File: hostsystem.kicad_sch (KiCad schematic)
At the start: 75 parts, among them J1001 TC2050, J1002 Conn_01x03_Pin, U1001 AM6231ASGGGAALW, U1002 SN74LVC2G241DCUR, U1003 AT24C32D-STUM-T, X1001 32.768kHz, X1002 25MHz

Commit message: Added almost all passive component footprints
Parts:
- C1001, C1005, C1007: footprint (none) -> Capacitor_SMD:C_0201_0603Metric
- C1002, C1003, C1004, C1006, C1008, C1009: footprint (none) -> Capacitor_SMD:C_0402_1005Metric
- D1001, D1004, D1005, D1006: footprint (none) -> Diode_SMD:D_SOD-523
- D1002, D1003: footprint (none) -> Diode_SMD:D_SOD-882
- R1001, R1002, R1003, R1004, R1005, R1006, R1007, R1008, R1009, R1010, R1012, R1013, R1014, R1015, R1048, R1049, R1050, R1051: footprint (none) -> Resistor_SMD:R_0402_1005Metric
- R1011, R1016, R1017, R1018, R1019, R1020, R1021, R1022, R1023, R1024, R1025, R1026, R1027, R1028, R1029, R1030, R1031, R1032, R1033, R1034, R1035, R1036, R1037, R1038, R1039, R1040, R1041, R1042, R1043, R1044, R1045, R1046, R1047: footprint (none) -> Resistor_SMD:R_0201_0603Metric
- TP1001, TP1002: footprint (none) -> TestPoint:TestPoint_Pad_1.0x1.0mm
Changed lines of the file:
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@@
 			)
 		)
-		(property "Footprint" ""
+		(property "Footprint" "Resistor_SMD:R_0201_0603Metric"
 			(at 617.982 49.53 90)
 			(effects
@@
 			)
 		)
-		(property "Footprint" ""
+		(property "Footprint" "Resistor_SMD:R_0402_1005Metric"
 			(at 85.852 92.71 90)
 			(effects
@@
 			)
 		)
-		(property "Footprint" ""
+		(property "Footprint" "Resistor_SMD:R_0402_1005Metric"
 			(at 140.462 388.62 90)
 			(effects
@@
 			)
 		)
-		(property "Footprint" ""
+		(property "Footprint" "Resistor_SMD:R_0402_1005Metric"
 			(at 455.422 49.53 90)
 			(effects
@@
 			)
 		)
-		(property "Footprint" ""
+		(property "Footprint" "Resistor_SMD:R_0201_0603Metric"
 			(at 546.862 109.22 90)
 			(effects
@@
 			)
 		)
-		(property "Footprint" ""
+		(property "Footprint" "Resistor_SMD:R_0201_0603Metric"
 			(at 597.662 109.22 90)
 			(effects
@@
 			)
 		)
-		(property "Footprint" ""
+		(property "Footprint" "Resistor_SMD:R_0201_0603Metric"
 			(at 557.022 109.22 90)
 			(effects
@@
 			)
 		)
-		(property "Footprint" ""
+		(property "Footprint" "Diode_SMD:D_SOD-523"
 			(at 483.87 68.58 0)
 			(effects
@@
 			)
 		)
-		(property "Footprint" ""
+		(property "Footprint" "TestPoint:TestPoint_Pad_1.0x1.0mm"
 			(at 99.06 97.79 0)
 			(effects
@@
 			)
 		)
-		(property "Footprint" ""
+		(property "Footprint" "Resistor_SMD:R_0201_0603Metric"
 			(at 607.822 49.53 90)
 			(effects
@@
 			)
 		)
-		(property "Footprint" ""
+		(property "Footprint" "Capacitor_SMD:C_0402_1005Metric"
 			(at 191.4652 325.12 0)
 			(effects
@@
 			)
 		)
-		(property "Footprint" ""
+		(property "Footprint" "Resistor_SMD:R_0402_1005Metric"
 			(at 466.09 95.758 90)
 			(effects
@@
 			)
 		)
-		(property "Footprint" ""
+		(property "Footprint" "Resistor_SMD:R_0201_0603Metric"
 			(at 678.942 49.53 90)
 			(effects
@@
 			)
 		)
-		(property "Footprint" ""
+		(property "Footprint" "Resistor_SMD:R_0402_1005Metric"
 			(at 466.09 70.358 90)
 			(effects
@@
 			)
 		)
-		(property "Footprint" ""
+		(property "Footprint" "Resistor_SMD:R_0201_0603Metric"
 			(at 648.462 109.22 90)
 			(effects
@@
 			)
 		)
-		(property "Footprint" ""
+		(property "Footprint" "Capacitor_SMD:C_0402_1005Metric"
 			(at 204.47 188.2648 0)
 			(effects
@@
 			)
 		)
-		(property "Footprint" ""
+		(property "Footprint" "Resistor_SMD:R_0201_0603Metric"
 			(at 567.182 109.22 90)
 			(effects
@@
 			)
 		)
-		(property "Footprint" ""
+		(property "Footprint" "Resistor_SMD:R_0201_0603Metric"
 			(at 668.782 49.53 90)
 			(effects
@@
 			)
 		)
-		(property "Footprint" ""
+		(property "Footprint" "Resistor_SMD:R_0402_1005Metric"
 			(at 151.892 388.62 90)
 			(effects
@@
 			)
 		)
-		(property "Footprint" ""
+		(property "Footprint" "Resistor_SMD:R_0201_0603Metric"
 			(at 587.502 109.22 90)
 			(effects
@@
 			)
 		)
-		(property "Footprint" ""
+		(property "Footprint" "Diode_SMD:D_SOD-523"
 			(at 483.87 93.98 0)
 			(effects
@@
 			)
 		)
-		(property "Footprint" ""
+		(property "Footprint" "Resistor_SMD:R_0201_0603Metric"
 			(at 536.702 49.53 90)
 			(effects
@@
 			)
 		)
-		(property "Footprint" ""
+		(property "Footprint" "Resistor_SMD:R_0402_1005Metric"
 			(at 399.542 166.37 90)
 			(effects
@@
 			)
 		)
-		(property "Footprint" ""
+		(property "Footprint" "Resistor_SMD:R_0201_0603Metric"
 			(at 607.822 109.22 90)
 			(effects
@@
 			)
 		)
-		(property "Footprint" ""
+		(property "Footprint" "Resistor_SMD:R_0402_1005Metric"
 			(at 336.042 420.37 90)
 			(effects
@@
 			)
 		)
-		(property "Footprint" ""
+		(property "Footprint" "Resistor_SMD:R_0201_0603Metric"
 			(at 628.142 109.22 90)
 			(effects
@@
 			)
 		)
-		(property "Footprint" ""
+		(property "Footprint" "Resistor_SMD:R_0201_0603Metric"
 			(at 628.142 49.53 90)
 			(effects
@@
 			)
 		)
-		(property "Footprint" ""
+		(property "Footprint" "Resistor_SMD:R_0402_1005Metric"
 			(at 466.09 90.678 90)
 			(effects
@@
 			)
 		)
-		(property "Footprint" ""
+		(property "Footprint" "Resistor_SMD:R_0201_0603Metric"
 			(at 526.542 49.53 90)
 			(effects
@@
 			)
 		)
-		(property "Footprint" ""
+		(property "Footprint" "Resistor_SMD:R_0201_0603Metric"
 			(at 668.782 109.22 90)
 			(effects
@@
 			)
 		)
-		(property "Footprint" ""
+		(property "Footprint" "Resistor_SMD:R_0402_1005Metric"
 			(at 214.122 388.62 90)
 			(effects
@@
 			)
 		)
-		(property "Footprint" ""
+		(property "Footprint" "Resistor_SMD:R_0201_0603Metric"
 			(at 567.182 49.53 90)
 			(effects
@@
 			)
 		)
-		(property "Footprint" ""
+		(property "Footprint" "Resistor_SMD:R_0201_0603Metric"
 			(at 658.622 109.22 90)
 			(effects
@@
 			)
 		)
-		(property "Footprint" ""
+		(property "Footprint" "Diode_SMD:D_SOD-882"
 			(at 455.93 419.1 0)
 			(effects
@@
 			)
 		)
-		(property "Footprint" ""
+		(property "Footprint" "Capacitor_SMD:C_0402_1005Metric"
 			(at 173.6852 325.12 0)
 			(effects
@@
 			)
 		)
-		(property "Footprint" ""
+		(property "Footprint" "Resistor_SMD:R_0201_0603Metric"
 			(at 526.542 109.22 90)
 			(effects
@@
 			)
 		)
-		(property "Footprint" ""
+		(property "Footprint" "Resistor_SMD:R_0402_1005Metric"
 			(at 225.552 388.62 90)
 			(effects
@@
 			)
 		)
-		(property "Footprint" ""
+		(property "Footprint" "Resistor_SMD:R_0402_1005Metric"
 			(at 336.042 407.67 90)
 			(effects
@@
 			)
 		)
-		(property "Footprint" ""
+		(property "Footprint" "Resistor_SMD:R_0402_1005Metric"
 			(at 236.982 388.62 90)
 			(effects
@@
 			)
 		)
-		(property "Footprint" ""
+		(property "Footprint" "Resistor_SMD:R_0201_0603Metric"
 			(at 381 179.578 90)
 			(effects
@@
 			)
 		)
-		(property "Footprint" ""
+		(property "Footprint" "Resistor_SMD:R_0201_0603Metric"
 			(at 617.982 109.22 90)
 			(effects
@@
 			)
 		)
-		(property "Footprint" ""
+		(property "Footprint" "Resistor_SMD:R_0201_0603Metric"
 			(at 557.022 49.53 90)
 			(effects
@@
 			)
 		)
-		(property "Footprint" ""
+		(property "Footprint" "TestPoint:TestPoint_Pad_1.0x1.0mm"
 			(at 99.06 107.95 0)
 			(effects
@@
 			)
 		)
-		(property "Footprint" ""
+		(property "Footprint" "Capacitor_SMD:C_0201_0603Metric"
 			(at 174.9552 383.54 0)
 			(effects
@@
 			)
 		)
-		(property "Footprint" ""
+		(property "Footprint" "Resistor_SMD:R_0402_1005Metric"
 			(at 457.962 397.51 90)
 			(effects
@@
 			)
 		)
-		(property "Footprint" ""
+		(property "Footprint" "Resistor_SMD:R_0402_1005Metric"
 			(at 99.822 92.71 90)
 			(effects
@@
 			)
 		)
-		(property "Footprint" ""
+		(property "Footprint" "Capacitor_SMD:C_0402_1005Metric"
 			(at 204.47 228.9048 0)
 			(effects
@@
 			)
 		)
-		(property "Footprint" ""
+		(property "Footprint" "Diode_SMD:D_SOD-523"
 			(at 483.87 88.9 0)
 			(effects
@@
 			)
 		)
-		(property "Footprint" ""
+		(property "Footprint" "Resistor_SMD:R_0201_0603Metric"
 			(at 597.662 49.53 90)
 			(effects
@@
 			)
 		)
-		(property "Footprint" ""
+		(property "Footprint" "Diode_SMD:D_SOD-882"
 			(at 467.36 419.1 0)
 			(effects
@@
 			)
 		)
-		(property "Footprint" ""
+		(property "Footprint" "Capacitor_SMD:C_0402_1005Metric"
 			(at 204.47 175.5648 0)
 			(effects
@@
 			)
 		)
-		(property "Footprint" ""
+		(property "Footprint" "Resistor_SMD:R_0201_0603Metric"
 			(at 546.862 49.53 90)
 			(effects
@@
 			)
 		)
-		(property "Footprint" ""
+		(property "Footprint" "Resistor_SMD:R_0402_1005Metric"
 			(at 388.112 166.37 90)
 			(effects
@@
 			)
 		)
-		(property "Footprint" ""
+		(property "Footprint" "Resistor_SMD:R_0201_0603Metric"
 			(at 587.502 49.53 90)
 			(effects
@@
 			)
 		)
-		(property "Footprint" ""
+		(property "Footprint" "Capacitor_SMD:C_0402_1005Metric"
 			(at 204.47 216.2048 0)
 			(effects
@@
 			)
 		)
-		(property "Footprint" ""
+		(property "Footprint" "Resistor_SMD:R_0402_1005Metric"
 			(at 151.13 207.518 90)
 			(effects
@@
 			)
 		)
-		(property "Footprint" ""
+		(property "Footprint" "Resistor_SMD:R_0201_0603Metric"
 			(at 577.342 49.53 90)
 			(effects
@@
 			)
 		)
-		(property "Footprint" ""
+		(property "Footprint" "Diode_SMD:D_SOD-523"
 			(at 459.74 387.35 0)
 			(effects
@@
 			)
 		)
-		(property "Footprint" ""
+		(property "Footprint" "Resistor_SMD:R_0201_0603Metric"
 			(at 648.462 49.53 90)
 			(effects
@@
 			)
 		)
-		(property "Footprint" ""
+		(property "Footprint" "Capacitor_SMD:C_0201_0603Metric"
 			(at 350.2152 394.97 0)
 			(effects
@@
 			)
 		)
-		(property "Footprint" ""
+		(property "Footprint" "Resistor_SMD:R_0201_0603Metric"
 			(at 678.942 109.22 90)
 			(effects
@@
 			)
 		)
-		(property "Footprint" ""
+		(property "Footprint" "Resistor_SMD:R_0201_0603Metric"
 			(at 638.302 49.53 90)
 			(effects
@@
 			)
 		)
-		(property "Footprint" ""
+		(property "Footprint" "Resistor_SMD:R_0201_0603Metric"
 			(at 658.622 49.53 90)
 			(effects
@@
 			)
 		)
-		(property "Footprint" ""
+		(property "Footprint" "Resistor_SMD:R_0402_1005Metric"
 			(at 220.472 416.56 90)
 			(effects
@@
 			)
 		)
-		(property "Footprint" ""
+		(property "Footprint" "Resistor_SMD:R_0201_0603Metric"
 			(at 638.302 109.22 90)
 			(effects
@@
 			)
 		)
-		(property "Footprint" ""
+		(property "Footprint" "Resistor_SMD:R_0201_0603Metric"
 			(at 577.342 109.22 90)
 			(effects
@@
 			)
 		)
-		(property "Footprint" ""
+		(property "Footprint" "Capacitor_SMD:C_0201_0603Metric"
 			(at 424.18 396.5448 0)
 			(effects
@@
 			)
 		)
-		(property "Footprint" ""
+		(property "Footprint" "Resistor_SMD:R_0201_0603Metric"
 			(at 536.702 109.22 90)
 			(effects

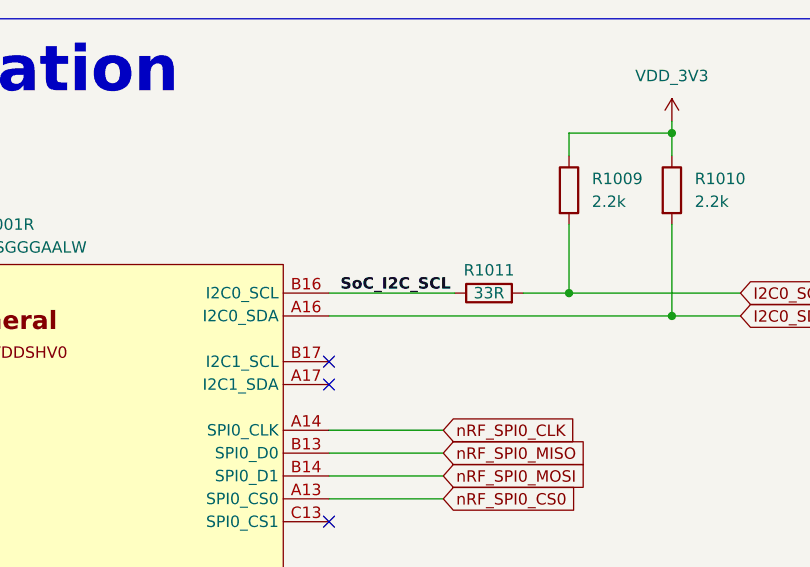
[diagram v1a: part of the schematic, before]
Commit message: Fixed footprint issues to comply with manufacturer constraints
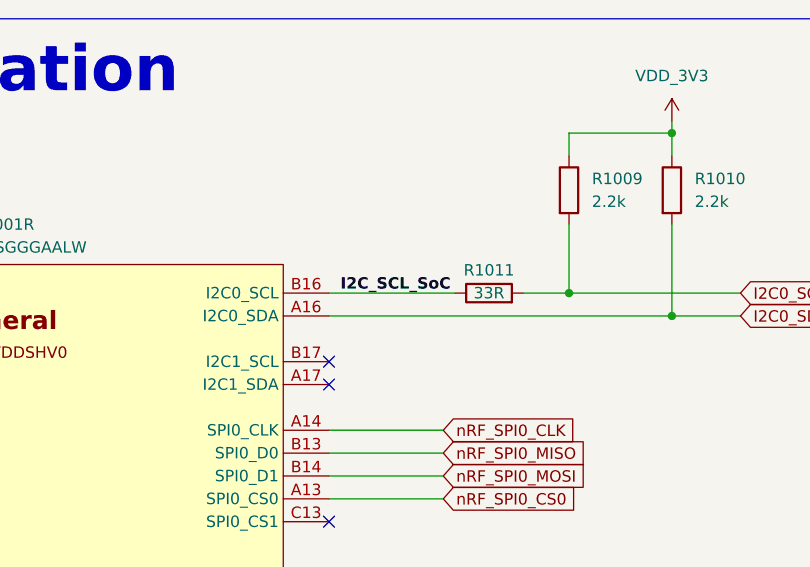
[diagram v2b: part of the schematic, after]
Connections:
- net SoC_I2C_SCL renamed I2C_SCL_SoC
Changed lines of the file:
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@@
 		)
 	)
-	(label "SoC_I2C_SCL"
+	(label "I2C_SCL_SoC"
 		(at 364.49 177.8 0)
 		(effects

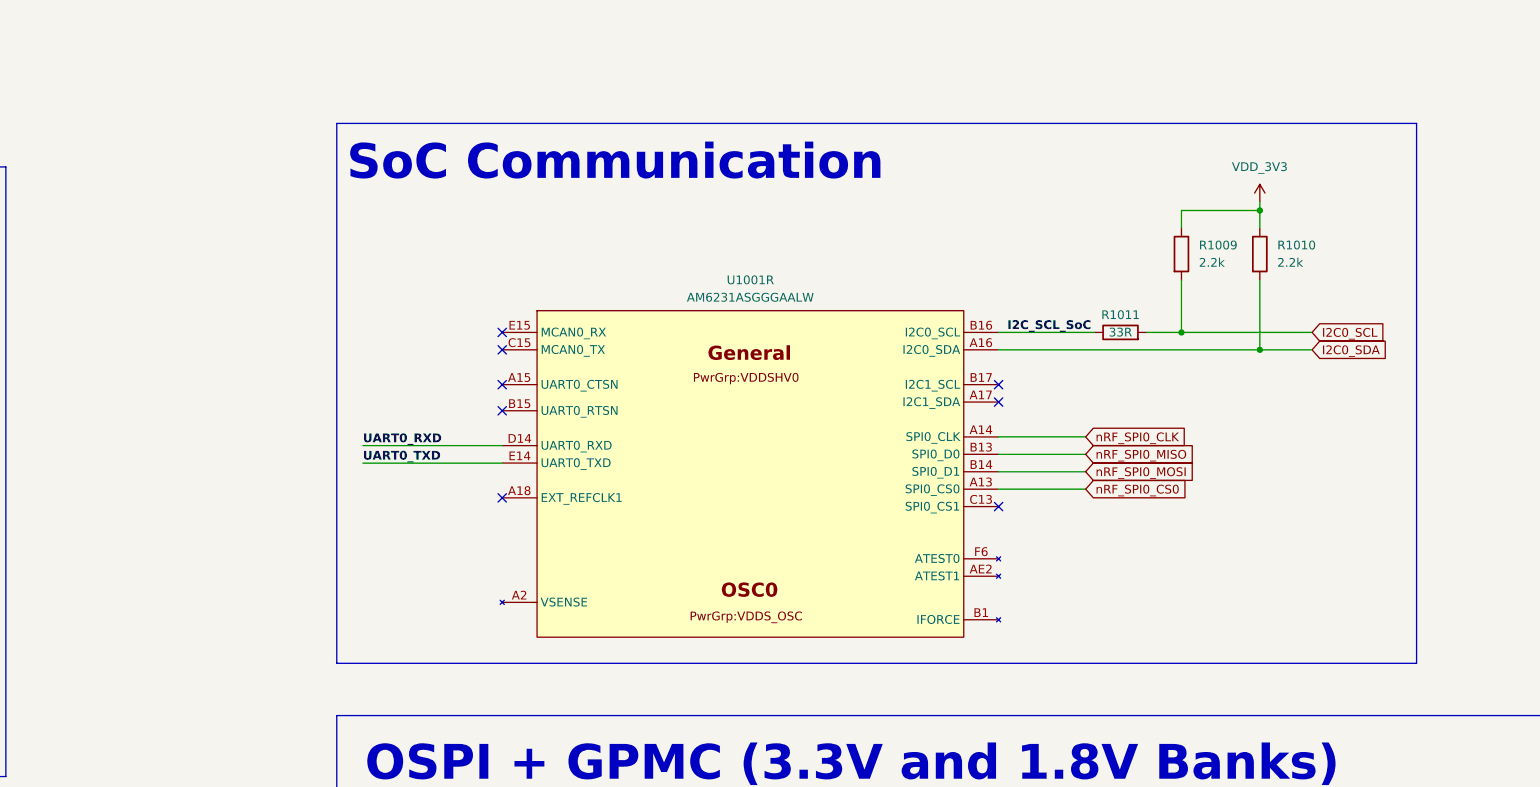
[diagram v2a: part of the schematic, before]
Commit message: Added necessary nRF52840 SPI logic circuitry and GPIOs. Also added pinmux
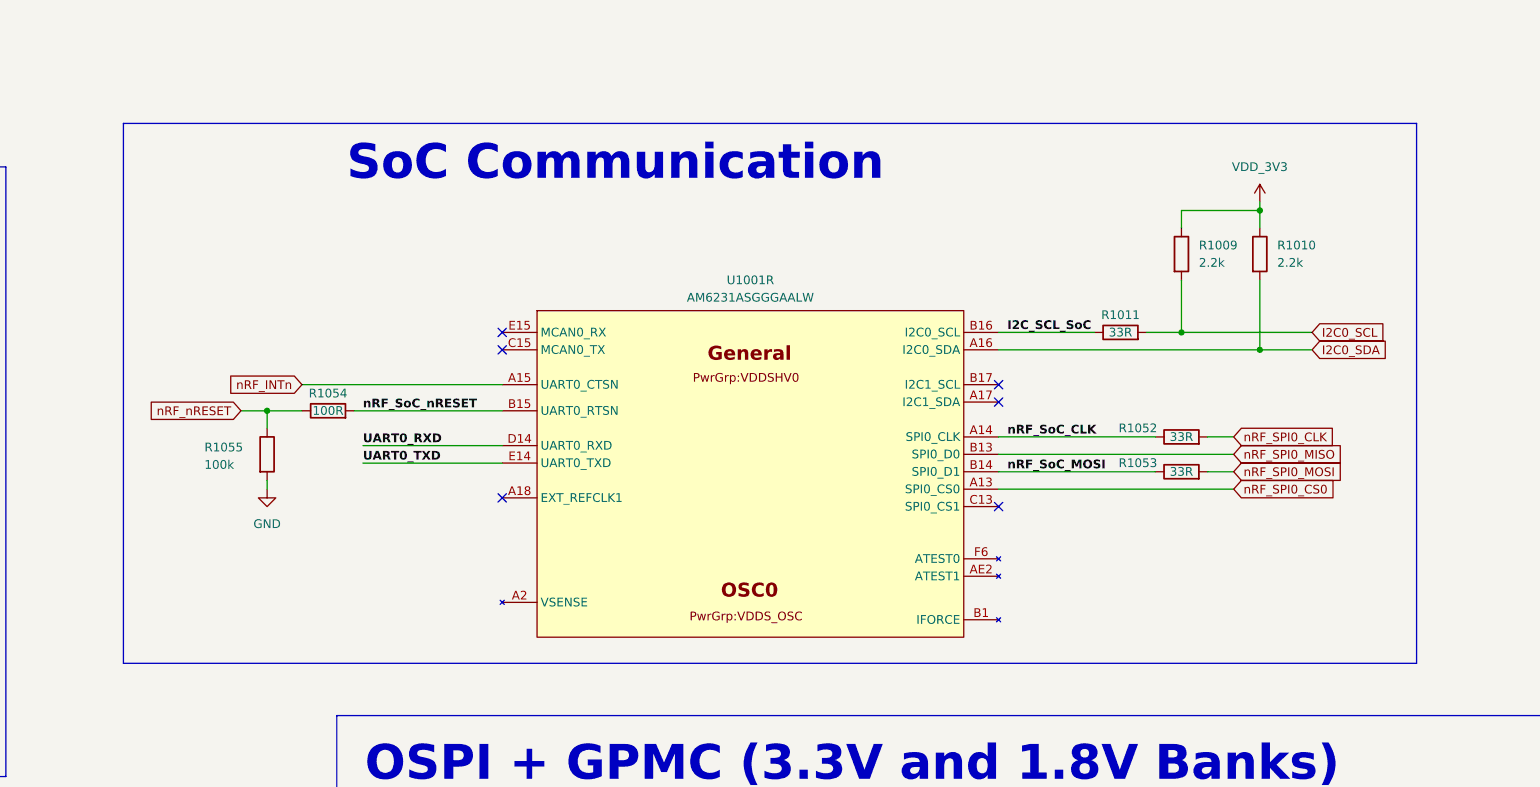
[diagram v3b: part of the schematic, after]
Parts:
- added R1052, R1053: 33R, Resistor_SMD:R_0201_0603Metric, symbol Device:R
- added R1054: 100R, symbol Device:R
- added R1055: 100k, symbol Device:R
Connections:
- net GND: now also R1055.2
- net nRF_SPI0_CLK: now also R1052.2; no longer U1001.A14 (SPI0_CLK)
- net nRF_SPI0_MOSI: now also R1053.2; no longer U1001.B14 (SPI0_D1)
- net nRF_INTn: now reaches U1001.A15 (UART0_CTSN)
- net nRF_SoC_nRESET: now reaches U1001.B15 (UART0_RTSN)
- net nRF_SoC_nRESET: now also R1054.2
- new net nRF_SoC_CLK: R1052.1, U1001.A14 (SPI0_CLK)
- new net nRF_SoC_MOSI: R1053.1, U1001.B14 (SPI0_D1)
- new net nRF_nRESET: R1054.1, R1055.1
- no-connect marks 105 -> 103

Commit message: Small fixes
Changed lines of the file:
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@@
 	(wire
 		(pts
-			(xy 393.7 193.04) (xy 397.51 193.04)
+			(xy 393.7 193.04) (xy 403.86 193.04)
 		)
 		(stroke
@@
 	(wire
 		(pts
-			(xy 393.7 198.12) (xy 397.51 198.12)
+			(xy 393.7 198.12) (xy 403.86 198.12)
 		)
 		(stroke
@@
 	(wire
 		(pts
-			(xy 363.22 195.58) (xy 397.51 195.58)
+			(xy 363.22 195.58) (xy 403.86 195.58)
 		)
 		(stroke
@@
 	(wire
 		(pts
-			(xy 363.22 200.66) (xy 397.51 200.66)
+			(xy 363.22 200.66) (xy 403.86 200.66)
 		)
 		(stroke
@@
 	(global_label "nRF_SPI0_MISO"
 		(shape input)
-		(at 397.51 195.58 0)
+		(at 403.86 195.58 0)
 		(fields_autoplaced yes)
 		(effects
@@
 		)
 		(property "Intersheetrefs" "${INTERSHEET_REFS}"
-			(at 414.828 195.58 0)
+			(at 421.178 195.58 0)
 			(effects
 				(font
@@
 	(global_label "nRF_SPI0_CLK"
 		(shape input)
-		(at 397.51 193.04 0)
+		(at 403.86 193.04 0)
 		(fields_autoplaced yes)
 		(effects
@@
 		)
 		(property "Intersheetrefs" "${INTERSHEET_REFS}"
-			(at 413.7999 193.04 0)
+			(at 420.1499 193.04 0)
 			(effects
 				(font
@@
 	(global_label "nRF_SPI0_MOSI"
 		(shape input)
-		(at 397.51 198.12 0)
+		(at 403.86 198.12 0)
 		(fields_autoplaced yes)
 		(effects
@@
 		)
 		(property "Intersheetrefs" "${INTERSHEET_REFS}"
-			(at 414.828 198.12 0)
+			(at 421.178 198.12 0)
 			(effects
 				(font
@@
 	(global_label "nRF_SPI0_CS0"
 		(shape input)
-		(at 397.51 200.66 0)
+		(at 403.86 200.66 0)
 		(fields_autoplaced yes)
 		(effects
@@
 		)
 		(property "Intersheetrefs" "${INTERSHEET_REFS}"
-			(at 413.9208 200.66 0)
+			(at 420.2708 200.66 0)
 			(effects
 				(font

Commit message: More SoC fanout
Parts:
- removed R1015: R, Resistor_SMD:R_0402_1005Metric, symbol Device:R
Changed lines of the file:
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@@
 	(wire
 		(pts
-			(xy 337.82 424.18) (xy 337.82 425.45)
-		)
-		(stroke
-			(width 0)
-			(type default)
-		)
-	)
-	(wire
-		(pts
 			(xy 322.58 303.53) (xy 304.8 303.53)
 		)
@@
 	(wire
 		(pts
-			(xy 337.82 414.02) (xy 337.82 416.56)
-		)
-		(stroke
-			(width 0)
-			(type default)
-		)
-	)
-	(wire
-		(pts
 			(xy 72.39 123.19) (xy 123.19 123.19)
 		)
@@
 	(symbol
 		(lib_id "Device:R")
-		(at 337.82 420.37 0)
-		(unit 1)
-		(exclude_from_sim no)
-		(in_bom yes)
-		(on_board yes)
-		(dnp yes)
-		(fields_autoplaced yes)
-		(property "Reference" "R1015"
-			(at 340.36 419.0999 0)
-			(effects
-				(font
-					(size 1.27 1.27)
-				)
-				(justify left)
-			)
-		)
-		(property "Value" "R"
-			(at 340.36 421.6399 0)
-			(effects
-				(font
-					(size 1.27 1.27)
-				)
-				(justify left)
-			)
-		)
-		(property "Footprint" "Resistor_SMD:R_0402_1005Metric"
-			(at 336.042 420.37 90)
-			(effects
-				(font
-					(size 1.27 1.27)
-				)
-				(hide yes)
-			)
-		)
-		(property "Datasheet" "~"
-			(at 337.82 420.37 0)
-			(effects
-				(font
-					(size 1.27 1.27)
-				)
-				(hide yes)
-			)
-		)
-		(property "Description" "Resistor"
-			(at 337.82 420.37 0)
-			(effects
-				(font
-					(size 1.27 1.27)
-				)
-				(hide yes)
-			)
-		)
-		(pin "1"
-		)
-		(pin "2"
-		)
-		(instances
-			(project "Leonhart"
-				(path "/b43b7bca-e50d-42ec-8ff0-e0016dfefe0a/5bbf73b3-d883-47e7-ac01-c5b0358ac807"
-					(reference "R1015")
-					(unit 1)
-				)
-			)
-		)
-	)
-	(symbol
-		(lib_id "Device:R")
 		(at 629.92 109.22 0)
 		(unit 1)
@@
 					(unit 1)
 				)
-			)
-		)
-	)
-	(symbol
-		(lib_id "power:GND")
-		(at 337.82 425.45 0)
-		(unit 1)
-		(exclude_from_sim no)
-		(in_bom yes)
-		(on_board yes)
-		(dnp no)
-		(fields_autoplaced yes)
-		(property "Reference" "#PWR01024"
-			(at 337.82 431.8 0)
-			(effects
-				(font
-					(size 1.27 1.27)
-				)
-				(hide yes)
-			)
-		)
-		(property "Value" "GND"
-			(at 337.82 430.53 0)
-			(effects
-				(font
-					(size 1.27 1.27)
-				)
-			)
-		)
-		(property "Footprint" ""
-			(at 337.82 425.45 0)
-			(effects
-				(font
-					(size 1.27 1.27)
-				)
-				(hide yes)
-			)
-		)
-		(property "Datasheet" ""
-			(at 337.82 425.45 0)
-			(effects
-				(font
-					(size 1.27 1.27)
-				)
-				(hide yes)
-			)
-		)
-		(property "Description" "Power symbol creates a global label with name \"GND\" , ground"
-			(at 337.82 425.45 0)
-			(effects
-				(font
-					(size 1.27 1.27)
-				)
-				(hide yes)
-			)
-		)
-		(pin "1"
-		)
-		(instances
-			(project "Leonhart"
-				(path "/b43b7bca-e50d-42ec-8ff0-e0016dfefe0a/5bbf73b3-d883-47e7-ac01-c5b0358ac807"
-					(reference "#PWR01024")
-					(unit 1)
-				)

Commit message: Cleaned up schematic
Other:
- note added: "SoC Bootstrap"
- moved on the sheet: D1004, D1005, D1006, R1016, R1017, R1018, R1019, R1020, R1021, R1022, R1023, R1024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

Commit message: Restarted SoC power decoupling based on manufacturer capabilities
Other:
- note added: "AM6231 SoC"
- moved on the sheet: C1001, C1002, C1003, C1004, C1005, C1006, C1007, C1008, C1009, D1001, D1002, D1003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
